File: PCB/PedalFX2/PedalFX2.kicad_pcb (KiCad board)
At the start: 2 copper layers, 55.5 x 42.5 mm, 12 parts, among them J1 Conn_01x04_Female, T1 ACJS-MHDR, T2 ACJS-MHDR, T3 54-00129

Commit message: Minor Tweaks
Minor tweaks to PCB
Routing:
- net Net-(SP1-Pad4): track 29.1 -> 31.2 mm
- net Net-(J1-Pad4): track 68.8 -> 70.4 mm
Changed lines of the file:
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@@
     (thickness 1.6)
     (drawings 20)
-    (tracks 73)
+    (tracks 75)
     (zones 0)
     (modules 12)
@@
     (solder_mask_min_width 0.25)
     (aux_axis_origin 0 0)
-    (visible_elements FFFFFF7F)
+    (visible_elements 7FFFFFFF)
     (pcbplotparams
       (layerselection 0x010fc_ffffffff)
@@
   (segment (start 145.288 109.982) (end 138.43 109.982) (width 1.2) (layer B.Cu) (net 2))
   (segment (start 138.43 109.982) (end 132.588 104.14) (width 1.2) (layer B.Cu) (net 2))
-  (segment (start 136.398 103.632) (end 135.128 102.362) (width 0.75) (layer F.Cu) (net 3))
-  (segment (start 142.24 103.632) (end 136.398 103.632) (width 0.75) (layer F.Cu) (net 3))
-  (segment (start 143.764 105.156) (end 142.24 103.632) (width 0.75) (layer F.Cu) (net 3))
-  (segment (start 134.28 140.462) (end 139.446 140.462) (width 0.75) (layer F.Cu) (net 3))
-  (segment (start 139.446 140.462) (end 141.166501 138.741499) (width 0.75) (layer F.Cu) (net 3))
-  (segment (start 131.318 137.5) (end 134.28 140.462) (width 0.75) (layer F.Cu) (net 3))
-  (segment (start 141.166501 138.741499) (end 141.166501 122.993499) (width 0.75) (layer F.Cu) (net 3))
-  (segment (start 141.166501 122.993499) (end 143.764 120.396) (width 0.75) (layer F.Cu) (net 3))
-  (segment (start 143.764 120.396) (end 143.764 105.156) (width 0.75) (layer F.Cu) (net 3))
   (segment (start 128.157 140.263) (end 119.888 140.263) (width 0.75) (layer F.Cu) (net 3))
   (segment (start 131.318 137.5) (end 128.555 140.263) (width 0.75) (layer F.Cu) (net 3))
   (segment (start 128.555 140.263) (end 128.157 140.263) (width 0.75) (layer F.Cu) (net 3))
+  (segment (start 136.398 103.632) (end 135.128 102.362) (width 0.75) (layer F.Cu) (net 3))
+  (segment (start 143.764 105.156) (end 142.24 103.632) (width 0.75) (layer F.Cu) (net 3))
+  (segment (start 137.287 140.462) (end 140.335 137.414) (width 0.75) (layer F.Cu) (net 3))
+  (segment (start 134.28 140.462) (end 137.287 140.462) (width 0.75) (layer F.Cu) (net 3))
+  (segment (start 140.335 137.414) (end 140.335 123.825) (width 0.75) (layer F.Cu) (net 3))
+  (segment (start 142.24 103.632) (end 136.398 103.632) (width 0.75) (layer F.Cu) (net 3))
+  (segment (start 131.318 137.5) (end 134.28 140.462) (width 0.75) (layer F.Cu) (net 3))
+  (segment (start 143.764 108.966) (end 143.764 105.156) (width 0.75) (layer F.Cu) (net 3))
+  (segment (start 136.906 115.824) (end 143.764 108.966) (width 0.75) (layer F.Cu) (net 3))
+  (segment (start 140.335 123.825) (end 136.906 120.396) (width 0.75) (layer F.Cu) (net 3))
+  (segment (start 136.906 120.396) (end 136.906 115.824) (width 0.75) (layer F.Cu) (net 3))
   (segment (start 126.238 127.42) (end 126.318 127.5) (width 0.25) (layer F.Cu) (net 4))
   (segment (start 126.318 128.858) (end 126.318 127.5) (width 0.25) (layer F.Cu) (net 4))
@@
   (segment (start 126.318 137.5) (end 124.038 137.5) (width 1.2) (layer F.Cu) (net 6))
   (segment (start 124.038 137.5) (end 120.396 133.858) (width 1.2) (layer F.Cu) (net 6))
-  (segment (start 137.207001 122.983001) (end 137.207001 116.792999) (width 0.75) (layer F.Cu) (net 7))
-  (segment (start 138.684 124.46) (end 137.207001 122.983001) (width 0.75) (layer F.Cu) (net 7))
-  (segment (start 137.207001 116.792999) (end 140.462 113.538) (width 0.75) (layer F.Cu) (net 7))
-  (segment (start 140.462 113.538) (end 140.462 106.314) (width 0.75) (layer F.Cu) (net 7))
-  (segment (start 138.684 130.134) (end 138.684 124.46) (width 0.75) (layer F.Cu) (net 7))
-  (segment (start 136.318 132.5) (end 138.684 130.134) (width 0.75) (layer F.Cu) (net 7))
+  (segment (start 136.318 132.5) (end 139.192 129.626) (width 0.75) (layer F.Cu) (net 7))
+  (segment (start 140.462 110.744) (end 140.462 106.314) (width 0.75) (layer F.Cu) (net 7))
+  (segment (start 135.255 115.951) (end 140.462 110.744) (width 0.75) (layer F.Cu) (net 7))
+  (segment (start 135.255 121.031) (end 135.255 115.951) (width 0.75) (layer F.Cu) (net 7))
+  (segment (start 139.192 124.968) (end 135.255 121.031) (width 0.75) (layer F.Cu) (net 7))
+  (segment (start 139.192 129.626) (end 139.192 124.968) (width 0.75) (layer F.Cu) (net 7))
   (segment (start 128.778 124.318) (end 122.174 117.714) (width 0.75) (layer F.Cu) (net 8))
   (segment (start 128.778 129.286) (end 128.778 124.318) (width 0.75) (layer F.Cu) (net 8))

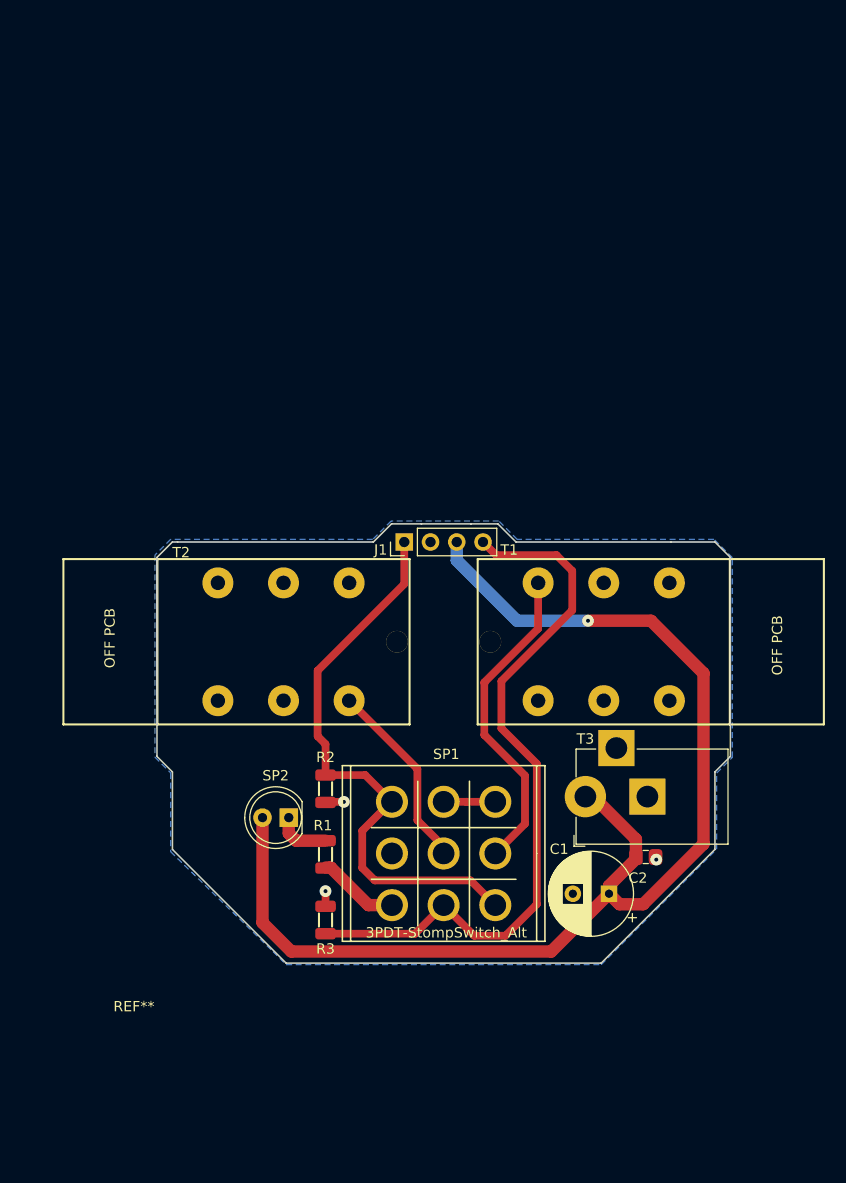
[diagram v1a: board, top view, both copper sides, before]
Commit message: Goofed
Goofed internal connector flipped and jacks not flush with housing. All fixed now, all boards redone.
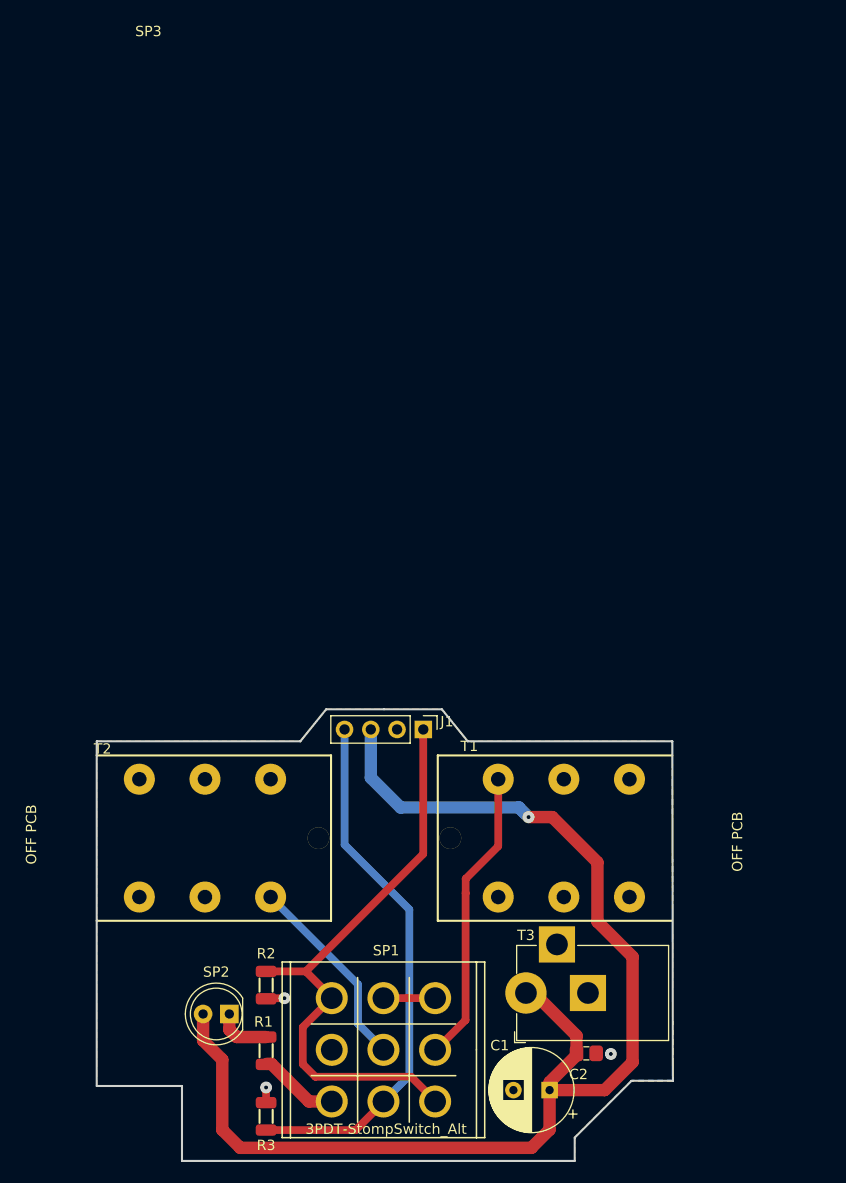
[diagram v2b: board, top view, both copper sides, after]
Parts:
- removed REF**: 1590B, KiCad Lib:1590B
- added SP3: Hammond_1590B, AVR-KiCAD-Lib-Special:1590B, F.Cu at (100.0, 161.0)
- moved T2 20.5 mm to (108.2, 131.0)
- moved SP1 19.9 mm to (125.5, 151.5)
- moved C1 19.9 mm to (141.6, 155.4)
- moved C2 19.9 mm to (145.1, 151.8)
- moved R1 19.9 mm to (114.1, 151.6)
- moved R2 19.9 mm to (114.1, 145.2)
- moved R3 19.9 mm to (114.1, 157.9)
- moved SP2 19.9 mm to (110.6, 148.0)
- moved T3 19.9 mm to (139.3, 146.0)
- moved T1 19.4 mm to (142.9, 131.0)
- moved J1 18.2 mm to (129.3, 120.5), turned to 270 degrees
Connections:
- net Net-(J1-Pad1) renamed /IN
- net Net-(J1-Pad4) renamed /OUT
- net Net-(SP1-Pad1) renamed /BYPASS
- net Net-(SP1-Pad4) renamed /Pedal_IN
- net Net-(SP1-Pad5) renamed /Pedal_OUT
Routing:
- net /OUT: track 70.4 -> 52.2 mm
- net +9V: track 118.8 -> 121.8 mm
- net /IN: track 57.3 -> 59.9 mm
- net /Pedal_IN: track 31.2 -> 28.8 mm
- net /Pedal_OUT: track 18.6 -> 19.3 mm
- added copper zone on F.Cu, net GND
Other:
- board size 55.5 x 42.5 mm -> 55.8 x 43.7 mm
- net class Default: clearance 0.2 -> 0.1524; trace_width 0.25 -> 0.1524; via_dia 0.8 -> 0.635; via_drill 0.4 -> 0.254
- rule trace_clearance: 0.2 -> 0.1524
- rule trace_min: 0.2 -> 0.1524
- rule via_min_drill: 0.3 -> 0.254
- rule via_min_size: 0.4 -> 0.635
